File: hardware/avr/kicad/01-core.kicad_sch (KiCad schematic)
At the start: 18 parts, among them U1 ATmega1284P-PU, Y1 8MHz

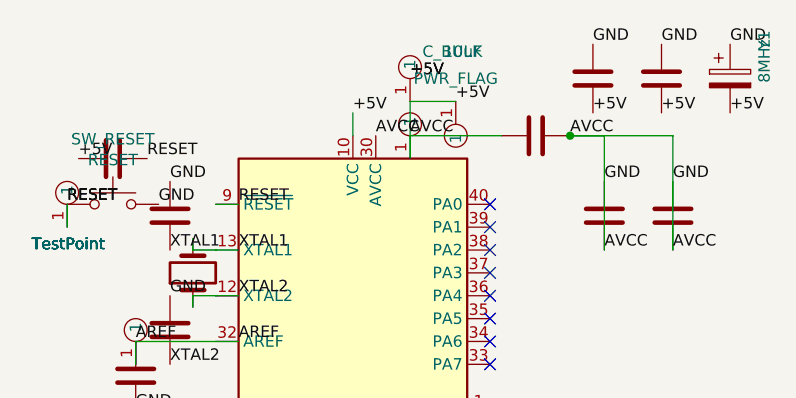
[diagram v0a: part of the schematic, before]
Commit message: Place AVR supply labels on actual pin endpoints
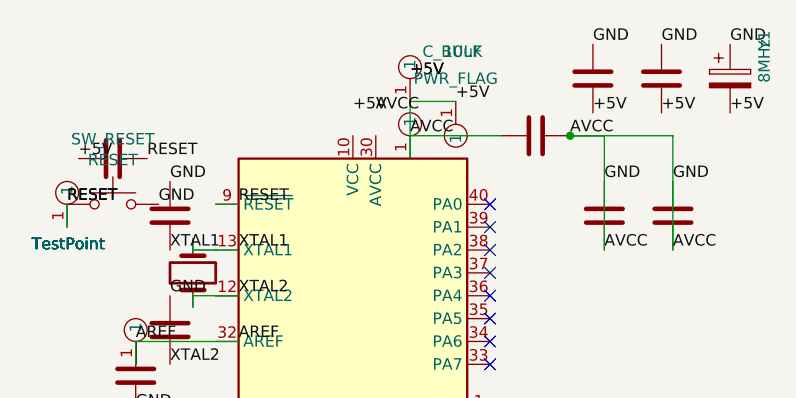
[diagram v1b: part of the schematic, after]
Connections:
- net +5V: no longer U1.10 (VCC), U1.30 (AVCC)
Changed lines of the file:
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@@
     (effects (font (size 1.27 1.27)) (justify left bottom))
   )
-  (wire (pts (xy 57.15 29.21) (xy 57.15 26.67))
-    (stroke (width 0) (type default))
-  )
-  (label "AVCC" (at 59.69 29.21 0) (fields_autoplaced)
+  (label "AVCC" (at 59.69 26.67 0) (fields_autoplaced)
     (effects (font (size 1.27 1.27)) (justify left bottom))
   )

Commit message: Restore AVR supply labels to verified ERC pin endpoints
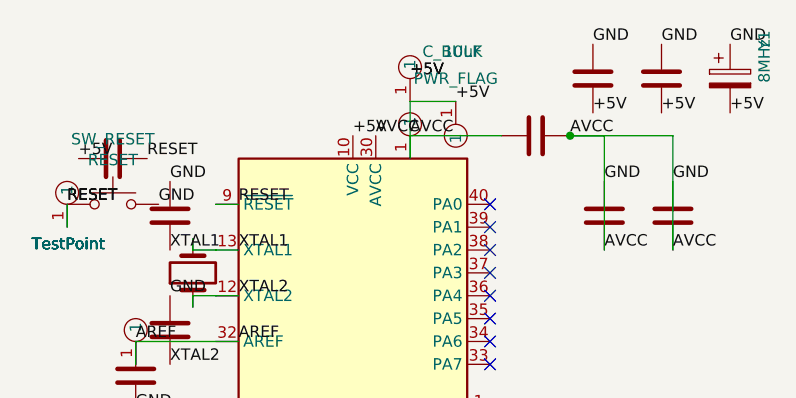
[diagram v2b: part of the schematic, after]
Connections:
- net +5V: now also U1.10 (VCC), U1.30 (AVCC)
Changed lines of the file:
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@@
 (kicad_sch (version 20230121) (generator eeschema)
   (paper "A4")
-  (label "+5V" (at 57.15 26.67 0) (fields_autoplaced)
+  (label "+5V" (at 57.15 29.21 0) (fields_autoplaced)
     (effects (font (size 1.27 1.27)) (justify left bottom))
   )
-  (label "AVCC" (at 59.69 26.67 0) (fields_autoplaced)
+  (label "AVCC" (at 59.69 29.21 0) (fields_autoplaced)
     (effects (font (size 1.27 1.27)) (justify left bottom))
   )
